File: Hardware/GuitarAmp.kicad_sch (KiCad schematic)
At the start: 9 parts, among them J1 NMJ4HFD2, U1 TL072

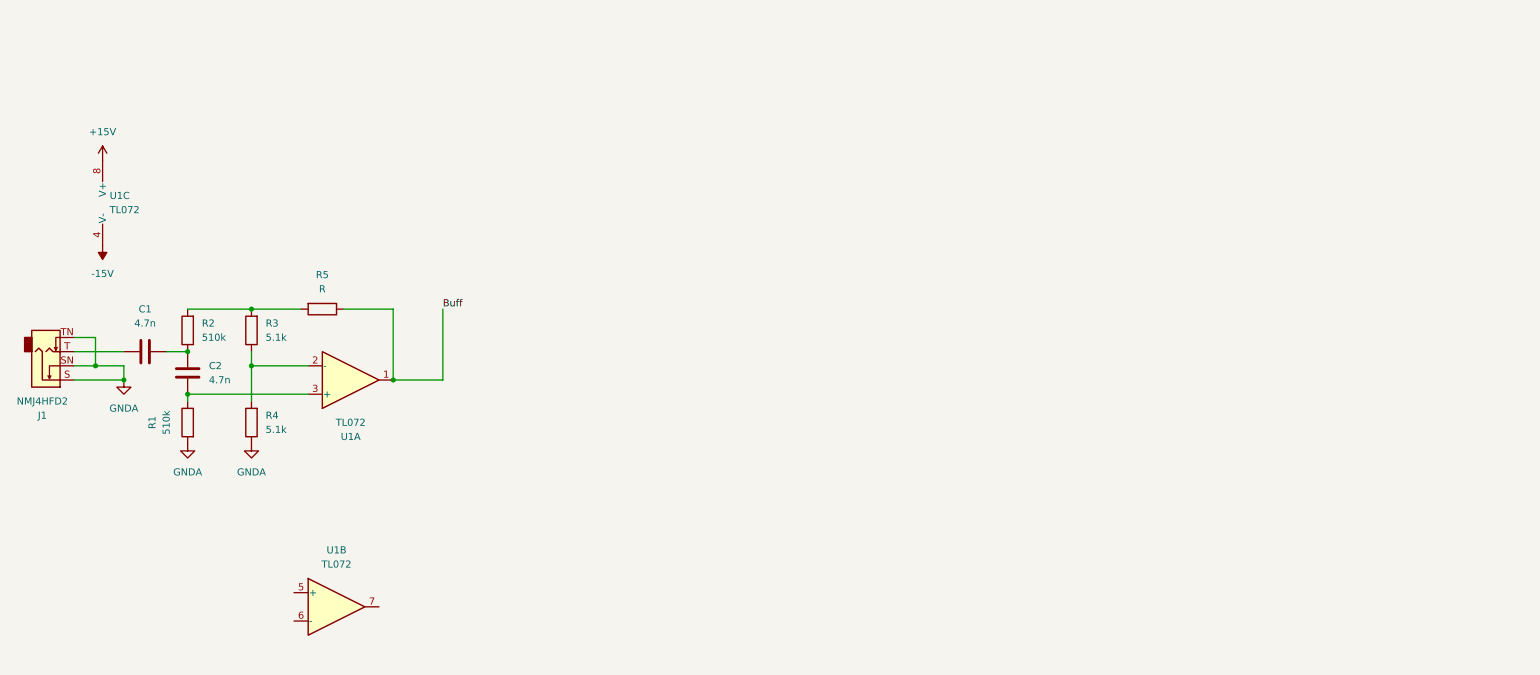
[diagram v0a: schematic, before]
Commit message: Upgraded Active TMB filter with wide band Ãpass filter
Signed-off-by: bebenlebricolo <benoittarrade@hotmail.fr>
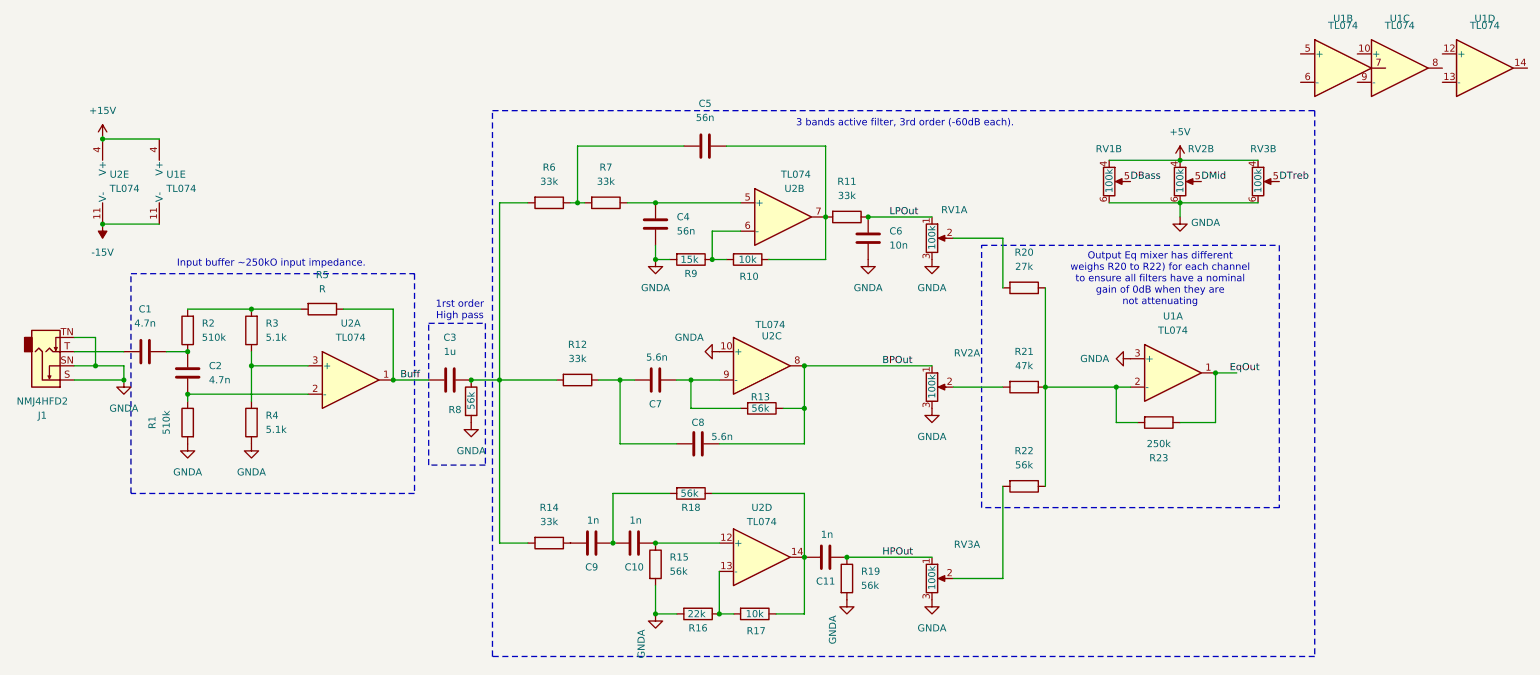
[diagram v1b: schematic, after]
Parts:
- removed U1: TL072, symbol Amplifier_Operational:TL072
- added C10, C11, C9: 1n, symbol Device:C
- added C3: 1u, symbol Device:C
- added C4, C5: 56n, symbol Device:C
- added C6: 10n, symbol Device:C
- added C7, C8: 5.6n, symbol Device:C
- added R10, R17: 10k, symbol Device:R
- added R11, R12, R14, R6, R7: 33k, symbol Device:R
- added R13, R15, R18, R19, R22, R8: 56k, symbol Device:R
- added R16: 22k, symbol Device:R
- added R20: 27k, symbol Device:R
- added R21: 47k, symbol Device:R
- added R23: 250k, symbol Device:R
- added R9: 15k, symbol Device:R
- added RV1, RV2, RV3: 100k, symbol Device:R_Potentiometer_Dual_Separate
- added U1, U2: TL074, symbol Amplifier_Operational:TL074
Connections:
- net +15V: now also U1.4 (V+), U2.4 (V+)
- net -15V: now also U1.11 (V-), U2.11 (V-)
- net Buff: now also C3.2, U2.1
- net GNDA: now also C4.2, C6.1, R15.2, R16.2, R19.2, R8.2, R9.2, RV1.3, RV1.6, RV2.3, RV2.6, RV3.3, RV3.6, U1.3 (+), U2.10 (+)
- net at R3.1, R4.2: now also U2.3 (+)
- net at C2.1, R1.1: now also U2.2 (-)
- new net: R20.1, R21.1, R22.1, R23.2, U1.2 (-)
- new net: C7.2, R13.2, U2.9 (-)
- new net: C11.1, R17.1, R18.1, U2.14
- new net: C10.1, C9.2, R18.2
- new net: C4.1, R7.1, U2.5 (+)
- new net: C10.2, R15.1, U2.12 (+)
- new net: R10.2, R9.1, U2.6 (-)
- new net: C7.1, C8.1, R12.1
- new net: C5.1, R6.1, R7.2
- new net: C5.2, R10.1, R11.2, U2.7
- new net: R21.2, RV2.2
- new net: R16.1, R17.2, U2.13 (-)
- new net: C3.1, R12.2, R14.2, R6.2, R8.1
- new net: R20.2, RV1.2
- new net: C9.1, R14.1
- new net: R22.2, RV3.2
- new net +5V: RV1.4, RV2.4, RV3.4
- new net BPOut: C8.2, R13.1, RV2.1, U2.8
- new net DBass: RV1.5
- new net DMid: RV2.5
- new net DTreb: RV3.5
- new net EqOut: R23.1, U1.1
- new net HPOut: C11.2, R19.1, RV3.1
- new net LPOut: C6.2, R11.1, RV1.1
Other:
- note added: "1rst order High pass"
- note added: "3 bands active filter, 3rd order (-60dB each)."
- note added: "Input buffer ~250kO input impedance."
- note added: "Output Eq mixer has different weighs R20 to R22) for each channel to ensure all filters have a nominal gain of 0dB when they are not attenuating"

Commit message: Updated Active eq sim and updated kicad schematic
Signed-off-by: bebenlebricolo <benoittarrade@hotmail.fr>
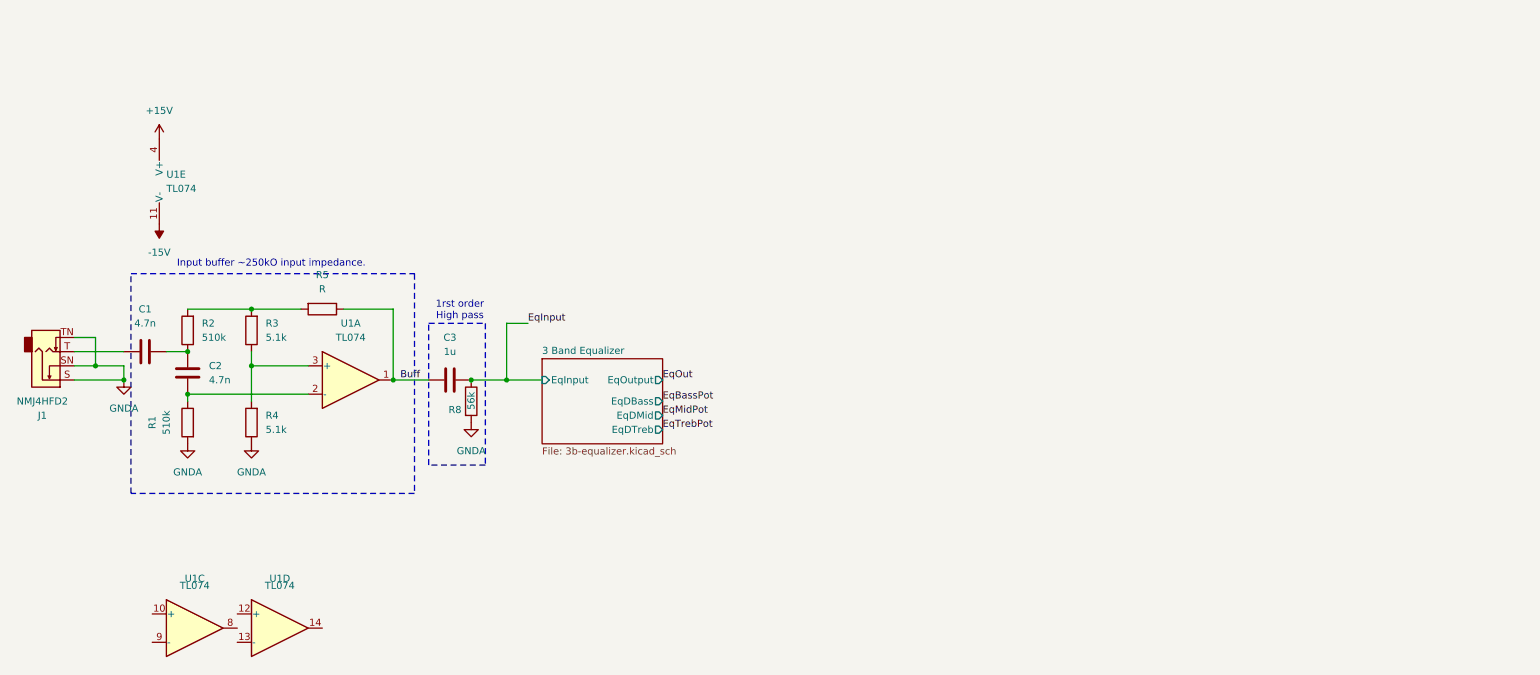
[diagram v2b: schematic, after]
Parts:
- removed C10, C11, C9: 1n, symbol Device:C
- removed C4, C5: 56n, symbol Device:C
- removed C6: 10n, symbol Device:C
- removed C7, C8: 5.6n, symbol Device:C
- removed R10, R17: 10k, symbol Device:R
- removed R11, R12, R14, R6, R7: 33k, symbol Device:R
- removed R13, R15, R18, R19, R22: 56k, symbol Device:R
- removed R16: 22k, symbol Device:R
- removed R20: 27k, symbol Device:R
- removed R21: 47k, symbol Device:R
- removed R23: 250k, symbol Device:R
- removed R9: 15k, symbol Device:R
- removed RV1, RV2, RV3: 100k, symbol Device:R_Potentiometer_Dual_Separate
- removed unit 2 of U1
- removed U2: TL074, symbol Amplifier_Operational:TL074
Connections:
- net Buff: now also U1.1
- net EqOut: no longer U1.1
- net GNDA: no longer U1.3 (+)
- net at U1.2 (-): now also C2.1, R1.1
- net at R3.1, R4.2: now also U1.3 (+)
- net EqInput: now reaches C3.1, R8.1
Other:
- added sheet 3 Band Equalizer (3b-equalizer.kicad_sch)
- note removed: "3 bands active filter, 3rd order (-60dB each)."
- note removed: "Output Eq mixer has different weighs R20 to R22) for each channel to ensure all filters have a nominal gain of 0dB when they are not attenuating"
- moved on the sheet: U1A, U1C, U1D

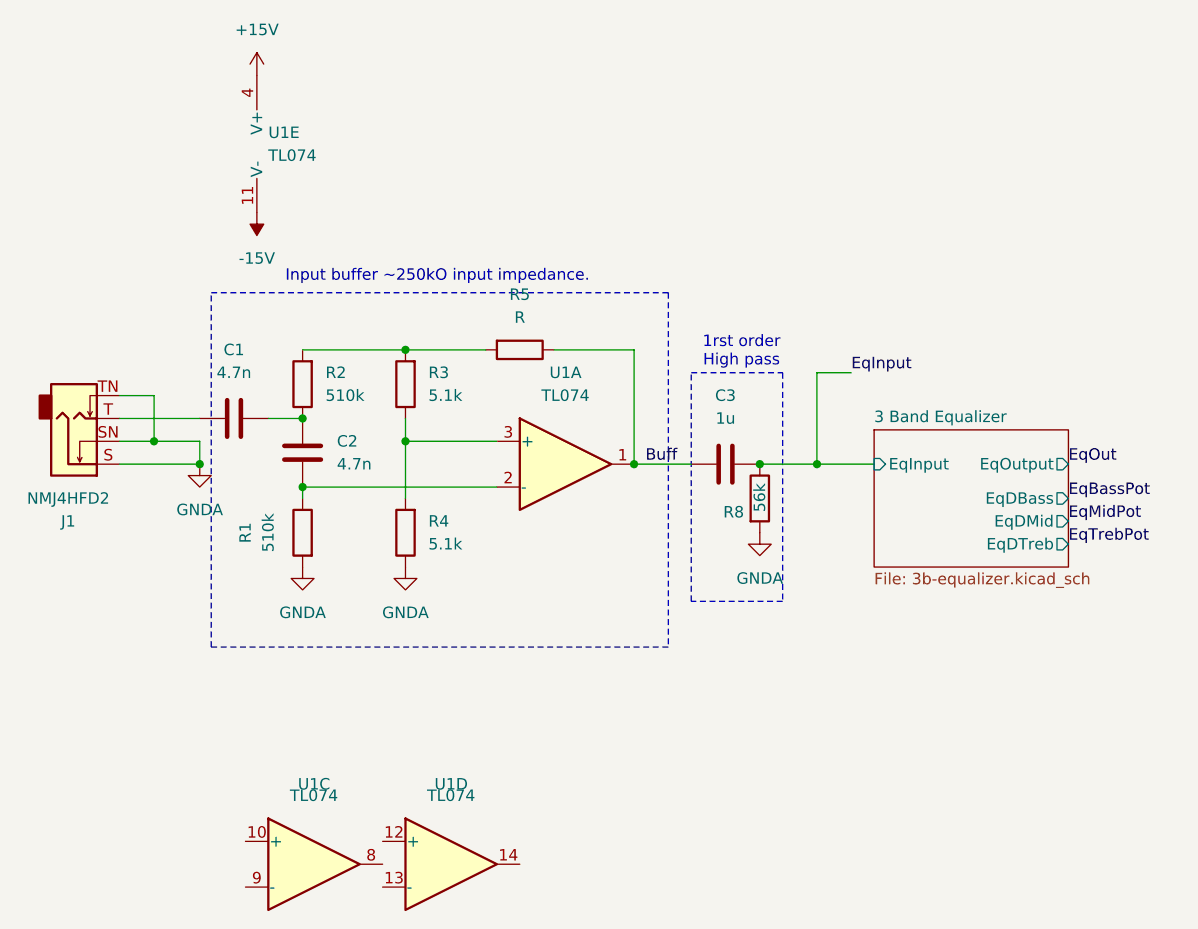
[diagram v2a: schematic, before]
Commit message: Calculated input impedance of buffer amp stage
Signed-off-by: bebenlebricolo <benoittarrade@hotmail.fr>
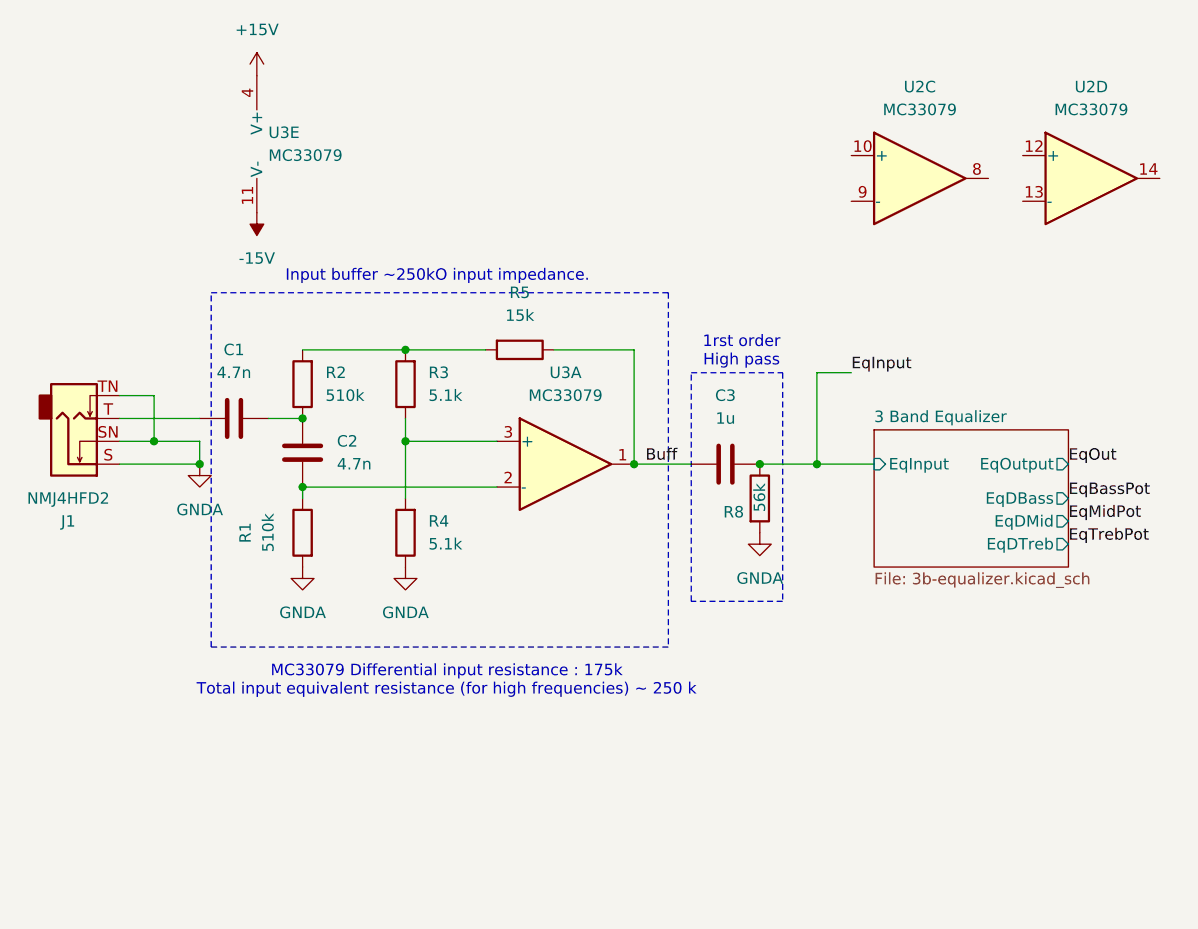
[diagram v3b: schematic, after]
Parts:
- removed U1: TL074, symbol Amplifier_Operational:TL074
- added U2, U3: MC33079, symbol Amplifier_Operational:MC33079
- R5: value R -> 15k
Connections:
- net +15V: now also U3.4 (V+)
- net -15V: now also U3.11 (V-)
- net Buff: now also U3.1
- net at C2.1, R1.1: now also U3.2 (-)
- net at R3.1, R4.2: now also U3.3 (+)
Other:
- note added: "MC33079 Differential input resistance : 175k Total input equivalent resistance (for high frequencies) ~ 250 k"
